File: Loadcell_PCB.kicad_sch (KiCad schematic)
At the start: 56 parts, among them J1 USB_C_Receptacle_USB2.0, J2 GPS, J3 Load cell side, J4 Micro_SD_Card, J5 PT, Q1 S8550, SW1 RESET, U1 ATmega328P-M, U2 CH340C, U3 HX711, U4 74125, U5 LD1117S33TR_SOT223, Y1 16MHz

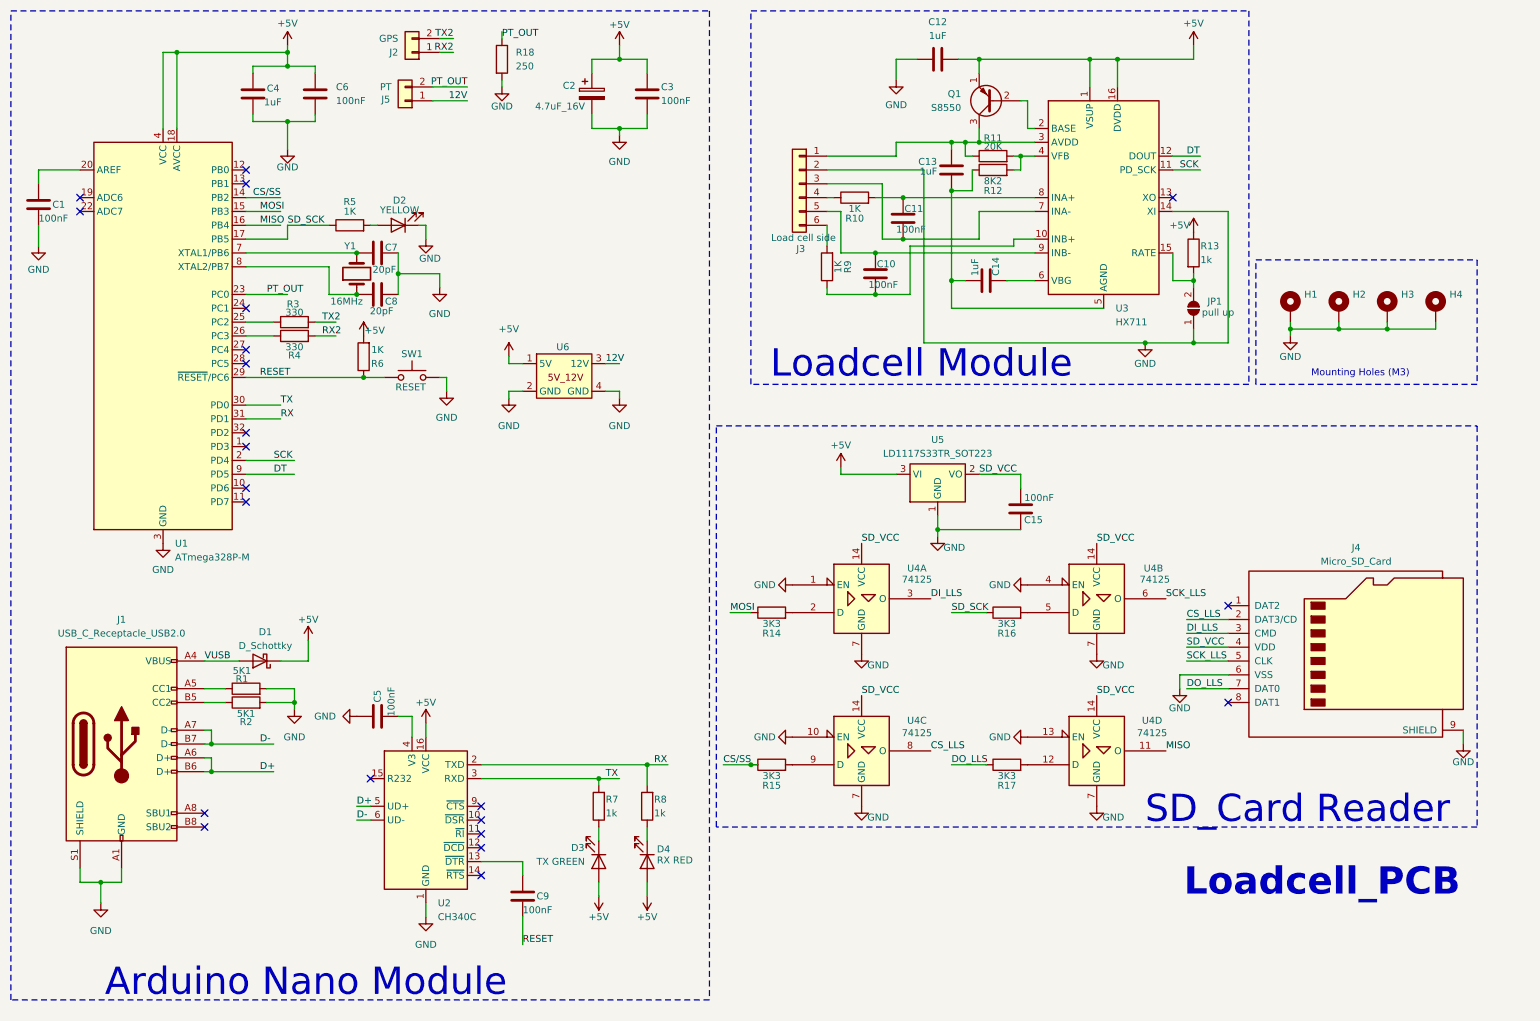
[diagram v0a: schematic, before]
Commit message: Re-layout progress at 15% and add connector pin for in system programming
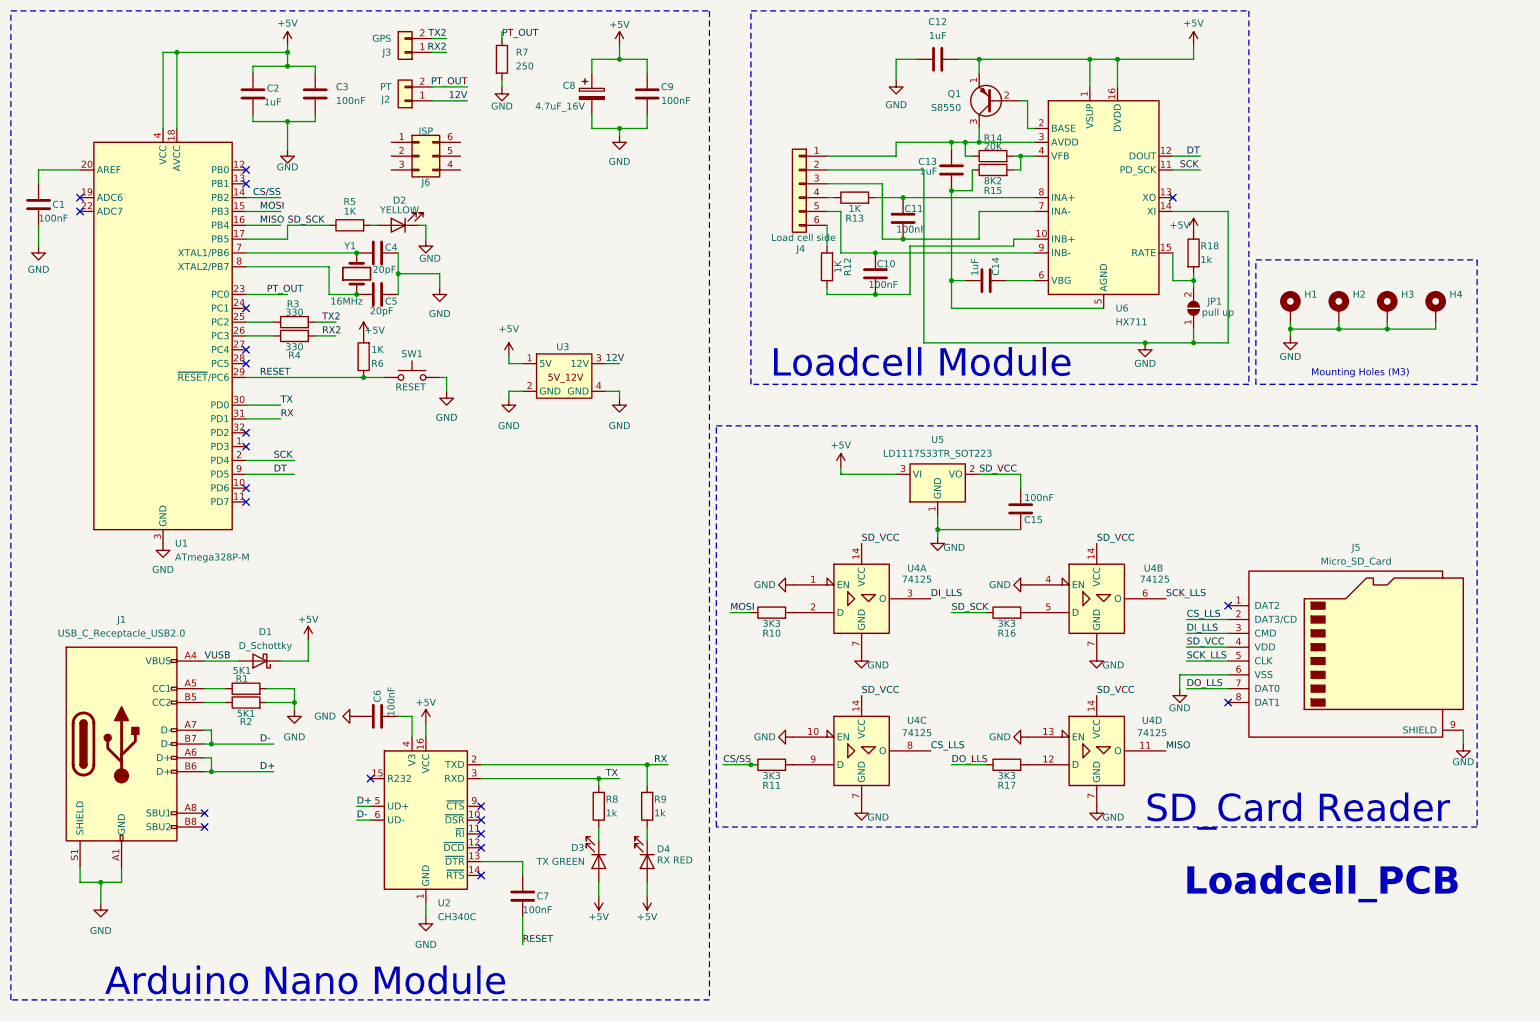
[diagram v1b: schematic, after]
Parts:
- added J6: ISP, Connector_PinHeader_1.27mm:PinHeader_2x03_P1.27mm_Vertical, symbol Connector_Generic:Conn_02x03_Counter_Clockwise
- renumbered C4 to C2, C6 to C3, C7 to C4, C8 to C5, C5 to C6, C9 to C7, C2 to C8, C3 to C9, J5 to J2, J2 to J3, J3 to J4, J4 to J5, R14 to R10, R15 to R11, R9 to R12, R10 to R13, R11 to R14, R12 to R15, R13 to R18, R18 to R7, R7 to R8, R8 to R9, U6 to U3, U3 to U6
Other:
- moved on the sheet: J3

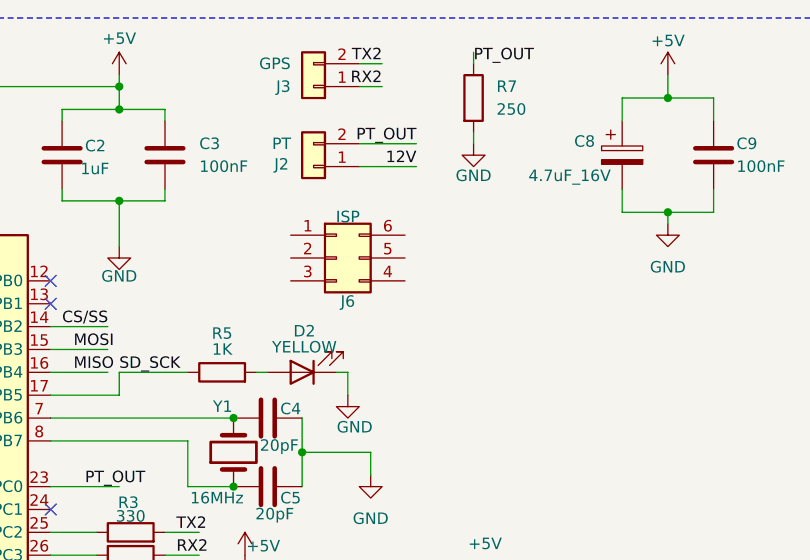
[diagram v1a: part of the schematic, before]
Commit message: Stage 1 layout and modify offset minimum raw number for PT
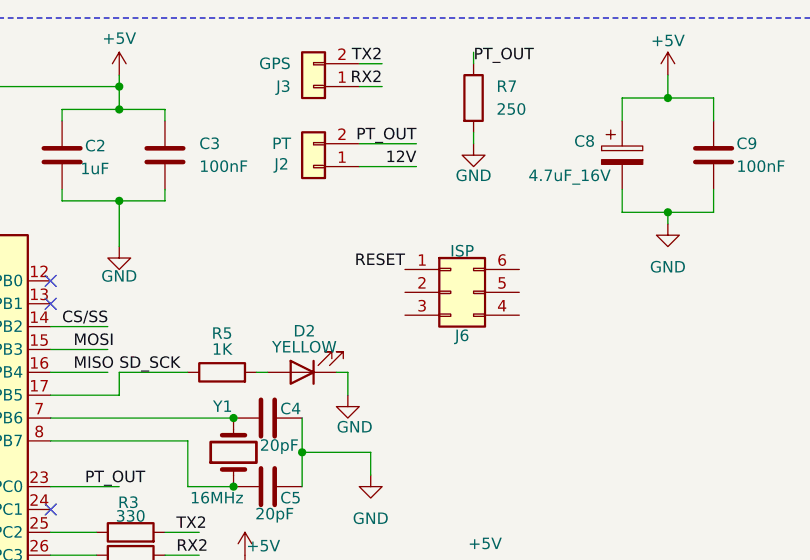
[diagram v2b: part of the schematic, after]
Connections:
- net RESET: now also J6.1 (Pin_1)
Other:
- moved on the sheet: J6
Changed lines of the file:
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@@
+		)
+	)
+	(label "RESET"
+		(at 96.52 41.91 180)
+		(fields_autoplaced yes)
+		(effects
+			(font
+				(size 1.27 1.27)
+			)
+			(justify right bottom)
 		)
 	)
@@
 	(symbol
 		(lib_id "Connector_Generic:Conn_02x03_Counter_Clockwise")
-		(at 88.9 40.64 0)
+		(at 101.6 44.45 0)
 		(unit 1)
 		(exclude_from_sim no)
@@
 		(dnp no)
 		(property "Reference" "J6"
-			(at 90.17 45.466 0)
+			(at 102.87 49.276 0)
 			(effects
 				(font
@@
 		)
 		(property "Value" "ISP"
-			(at 90.17 36.068 0)
+			(at 102.87 39.878 0)
 			(effects
 				(font
@@
 		)
 		(property "Footprint" "Connector_PinHeader_1.27mm:PinHeader_2x03_P1.27mm_Vertical"
-			(at 88.9 40.64 0)
+			(at 101.6 44.45 0)
 			(effects
 				(font
@@
 		)
 		(property "Datasheet" "~"
-			(at 88.9 40.64 0)
+			(at 101.6 44.45 0)
 			(effects
 				(font
@@
 		)
 		(property "Description" "Generic connector, double row, 02x03, counter clockwise pin numbering scheme (similar to DIP package numbering), script generated (kicad-library-utils/schlib/autogen/connector/)"
-			(at 88.9 40.64 0)
-			(effects
-				(font
+			(at 101.6 44.45 0)
+			(effects
+				(font

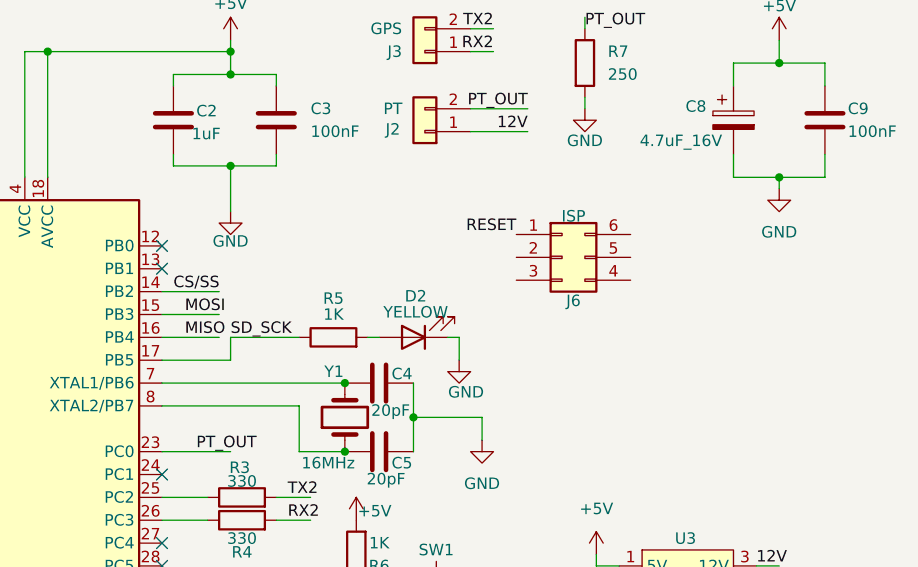
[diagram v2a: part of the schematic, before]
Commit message: Change PT formula for 1.1V analogRead
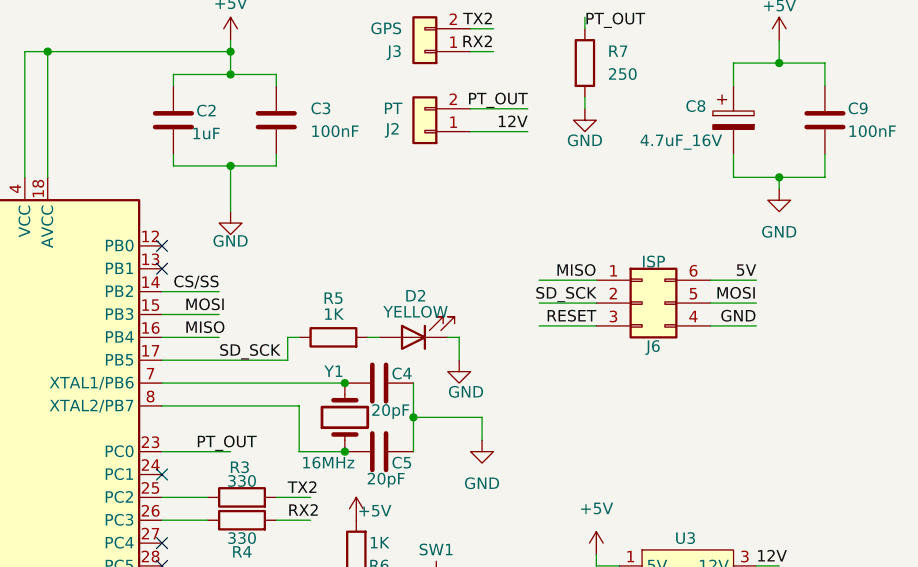
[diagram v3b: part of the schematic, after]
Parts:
- Y1: footprint Crystal:Crystal_SMD_HC49-SD_HandSoldering -> Crystal:Crystal_SMD_HC49-SD
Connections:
- net GND: now also J6.4 (Pin_4)
- net MISO: now also J6.1 (Pin_1)
- net MOSI: now also J6.5 (Pin_5)
- net RESET: now also J6.3 (Pin_3); no longer J6.1 (Pin_1)
- net SD_SCK: now also J6.2 (Pin_2)
- net 5V: now reaches J6.6 (Pin_6)
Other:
- moved on the sheet: J6
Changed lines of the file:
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@@
 	(wire
 		(pts
-			(xy 64.77 53.34) (xy 72.39 53.34)
-		)
-		(stroke
-			(width 0)
-			(type default)
-		)
-	)
-	(wire
-		(pts
 			(xy 227.33 58.42) (xy 227.33 63.5)
 		)
@@
 	(wire
 		(pts
+			(xy 99.06 49.53) (xy 105.41 49.53)
+		)
+		(stroke
+			(width 0)
+			(type default)
+		)
+	)
+	(wire
+		(pts
 			(xy 212.09 22.86) (xy 217.17 22.86)
 		)
@@
 	(wire
 		(pts
+			(xy 118.11 49.53) (xy 123.19 49.53)
+		)
+		(stroke
+			(width 0)
+			(type default)
+		)
+	)
+	(wire
+		(pts
 			(xy 120.65 33.02) (xy 120.65 35.56)
 		)
@@
 	(wire
 		(pts
+			(xy 99.06 52.07) (xy 105.41 52.07)
+		)
+		(stroke
+			(width 0)
+			(type default)
+		)
+	)
+	(wire
+		(pts
 			(xy 57.15 86.36) (xy 63.5 86.36)
 		)
@@
 	(wire
 		(pts
+			(xy 118.11 52.07) (xy 123.19 52.07)
+		)
+		(stroke
+			(width 0)
+			(type default)
+		)
+	)
+	(wire
+		(pts
 			(xy 257.81 72.39) (xy 266.7 72.39)
 		)
@@
 	(wire
 		(pts
+			(xy 99.06 46.99) (xy 105.41 46.99)
+		)
+		(stroke
+			(width 0)
+			(type default)
+		)
+	)
+	(wire
+		(pts
 			(xy 125.73 22.86) (xy 120.65 22.86)
 		)
@@
 	(wire
 		(pts
-			(xy 57.15 55.88) (xy 64.77 55.88)
+			(xy 57.15 55.88) (xy 71.12 55.88)
 		)
 		(stroke
@@
 	(wire
 		(pts
-			(xy 64.77 53.34) (xy 64.77 55.88)
-		)
-		(stroke
-			(width 0)
-			(type default)
-		)
-	)
-	(wire
-		(pts
 			(xy 181.61 74.93) (xy 222.25 74.93)
 		)
@@
 	(wire
 		(pts
+			(xy 118.11 46.99) (xy 123.19 46.99)
+		)
+		(stroke
+			(width 0)
+			(type default)
+		)
+	)
+	(wire
+		(pts
 			(xy 57.15 96.52) (xy 66.04 96.52)
 		)
@@
 	(wire
 		(pts
+			(xy 71.12 55.88) (xy 71.12 53.34)
+		)
+		(stroke
+			(width 0)
+			(type default)
+		)
+	)
+	(wire
+		(pts
 			(xy 125.73 35.56) (xy 125.73 36.83)
 		)
@@
 	(wire
 		(pts
+			(xy 71.12 53.34) (xy 72.39 53.34)
+		)
+		(stroke
+			(width 0)
+			(type default)
+		)
+	)
+	(wire
+		(pts
 			(xy 19.05 53.34) (xy 19.05 57.15)
 		)
@@
 		)
 	)
-	(label "PT_OUT"
-		(at 97.79 27.94 180)
+	(label "MOSI"
+		(at 123.19 49.53 180)
 		(fields_autoplaced yes)
 		(effects
@@
 		)
 	)
-	(label "RESET"
-		(at 96.52 41.91 180)
+	(label "PT_OUT"
+		(at 97.79 27.94 180)
 		(fields_autoplaced yes)
 		(effects
@@
 	)
 	(label "MISO"
+		(at 105.41 46.99 180)
+		(fields_autoplaced yes)
+		(effects
+			(font
+				(size 1.27 1.27)
+			)
+			(justify right bottom)
+		)
+	)
+	(label "MISO"
 		(at 59.69 53.34 0)
 		(fields_autoplaced yes)
@@
 	)
 	(label "SD_SCK"
-		(at 64.77 53.34 0)
+		(at 63.5 55.88 0)
 		(fields_autoplaced yes)
 		(effects
@@
 		)
 	)
+	(label "GND"
+		(at 123.19 52.07 180)
+		(fields_autoplaced yes)
+		(effects
+			(font
+				(size 1.27 1.27)
+			)
+			(justify right bottom)
+		)
+	)
 	(label "CS{slash}SS"
 		(at 58.42 48.26 0)
@@
 		)
 	)
+	(label "5V"
+		(at 123.19 46.99 180)
+		(fields_autoplaced yes)
+		(effects
+			(font
+				(size 1.27 1.27)
+			)
+			(justify right bottom)
+		)
+	)
 	(label "PT_OUT"
 		(at 60.96 66.04 0)
@@
 		)
 	)
+	(label "RESET"
+		(at 105.41 52.07 180)
+		(fields_autoplaced yes)
+		(effects
+			(font
+				(size 1.27 1.27)
+			)
+			(justify right bottom)
+		)
+	)
 	(label "D-"
 		(at 77.47 162.56 0)
@@
 		)
 	)
+	(label "SD_SCK"
+		(at 105.41 49.53 180)
+		(fields_autoplaced yes)
+		(effects
+			(font
+				(size 1.27 1.27)
+			)
+			(justify right bottom)
+		)
+	)
 	(label "RX"
 		(at 63.5 88.9 0)
@@
 			)
 		)
-		(property "Footprint" "Crystal:Crystal_SMD_HC49-SD_HandSoldering"
+		(property "Footprint" "Crystal:Crystal_SMD_HC49-SD"
 			(at 77.47 62.23 0)
 			(effects
@@
 	(symbol
 		(lib_id "Connector_Generic:Conn_02x03_Counter_Clockwise")
-		(at 101.6 44.45 0)
+		(at 110.49 49.53 0)
 		(unit 1)
 		(exclude_from_sim no)
@@
 		(dnp no)
 		(property "Reference" "J6"
-			(at 102.87 49.276 0)
+			(at 111.76 54.356 0)
 			(effects
 				(font
@@
 		)
 		(property "Value" "ISP"
-			(at 102.87 39.878 0)
+			(at 111.76 44.958 0)
 			(effects
 				(font
@@
 		)
 		(property "Footprint" "Connector_PinHeader_1.27mm:PinHeader_2x03_P1.27mm_Vertical"
-			(at 101.6 44.45 0)
+			(at 110.49 49.53 0)
 			(effects
 				(font
@@
 		)
 		(property "Datasheet" "~"
-			(at 101.6 44.45 0)
+			(at 110.49 49.53 0)
 			(effects
 				(font
@@
 		)
 		(property "Description" "Generic connector, double row, 02x03, counter clockwise pin numbering scheme (similar to DIP package numbering), script generated (kicad-library-utils/schlib/autogen/connector/)"
-			(at 101.6 44.45 0)
+			(at 110.49 49.53 0)
 			(effects
 				(font
